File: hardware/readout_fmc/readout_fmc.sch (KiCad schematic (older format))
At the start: 0 parts

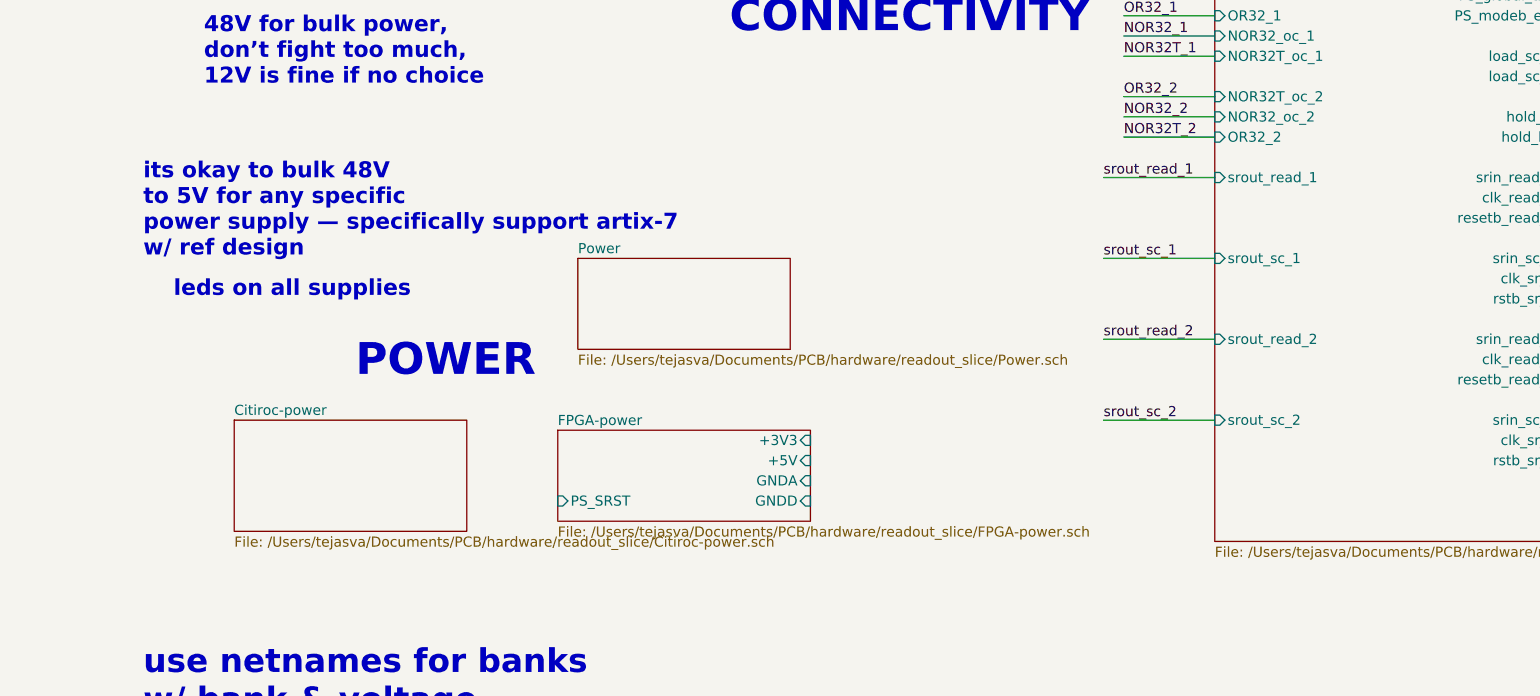
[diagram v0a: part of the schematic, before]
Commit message: SiPM Board RevC updated
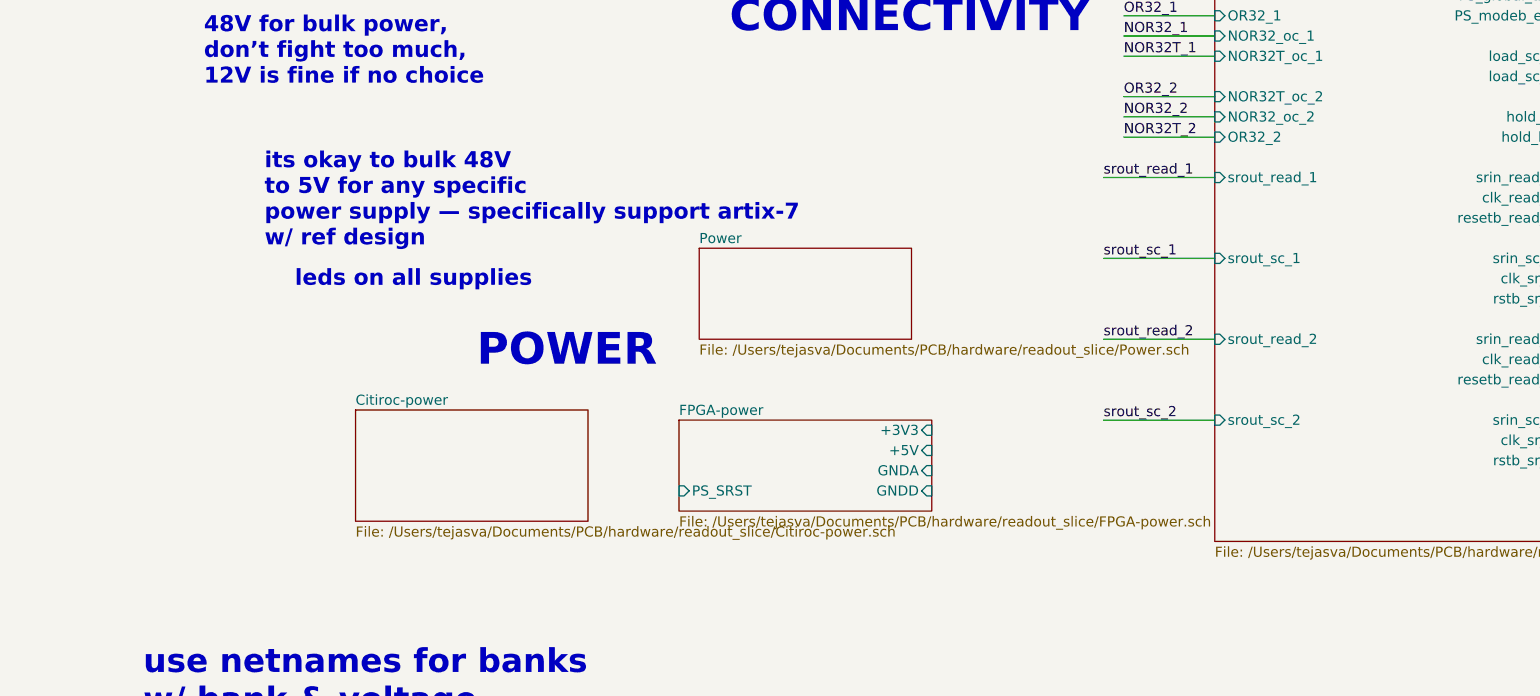
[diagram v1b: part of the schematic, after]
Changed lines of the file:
@@
 $EndSheet
 $Sheet
-S 2750 3750 1250 450
+S 3350 3700 1250 450
 U 6076C700
 F0 "FPGA-power" 50
 F1 "/Users/tejasva/Documents/PCB/hardware/readout_slice/FPGA-power.sch" 0
-F2 "PS_SRST" I L 2750 4100 50
-F3 "+3V3" I R 4000 3800 50
-F4 "+5V" I R 4000 3900 50
-F5 "GNDA" I R 4000 4000 50
-F6 "GNDD" I R 4000 4100 50
-$EndSheet
-$Sheet
-S 1150 3700 1150 550
+F2 "PS_SRST" I L 3350 4050 50
+F3 "+3V3" I R 4600 3750 50
+F4 "+5V" I R 4600 3850 50
+F5 "GNDA" I R 4600 3950 50
+F6 "GNDD" I R 4600 4050 50
+$EndSheet
+$Sheet
+S 1750 3650 1150 550
 U 607ECAFE
 F0 "Citiroc-power" 50
 F1 "/Users/tejasva/Documents/PCB/hardware/readout_slice/Citiroc-power.sch" 50
 $EndSheet
-Text Notes 1750 3500 0    157  ~ 31
+Text Notes 2350 3450 0    157  ~ 31
 POWER
 Text Notes 7750 800  0    157  ~ 31
 CITIROC-FPGA
-Text Notes 850  3100 0    79   ~ 16
+Text Notes 1450 3050 0    79   ~ 16
 leds on all supplies
 Text Notes 1000 2050 0    79   ~ 16
@@
 F40 "3v3_GPIO4" I L 6000 1500 50
 $EndSheet
-Text Notes 700  2900 0    79   ~ 16
+Text Notes 1300 2850 0    79   ~ 16
 its okay to bulk 48V \nto 5V for any specific \npower supply — specifically support artix-7 \nw/ ref design
 Text Label 10950 4350 2    50   ~ 0
@@
 CONNECTIVITY
 $Sheet
-S 2850 2900 1050 450
+S 3450 2850 1050 450
 U 62251D77
 F0 "Power" 50

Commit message: Backplane Prototype RevC made
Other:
- note added: "CITIROC-FMC"
- note added: "Diff schematics for power, signals etc.\n\n"
- note removed: "CITIROC-FPGA"
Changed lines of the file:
@@
 POWER
 Text Notes 7750 800  0    157  ~ 31
-CITIROC-FPGA
+CITIROC-FMC
 Text Notes 1450 3050 0    79   ~ 16
 leds on all supplies
@@
 Wire Wire Line
 	8100 3800 7750 3800
+Text Notes 5600 6000 0    50   ~ 0
+Diff schematics for power, signals etc.\n\n
 $EndSCHEMATC
